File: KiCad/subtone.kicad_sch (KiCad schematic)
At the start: 10 parts, among them J1 7P Header, J2 Conn_01x07_Pin, J3 3P Header, SW1 Encoder, U1 MODULE-XIAO-RP2040

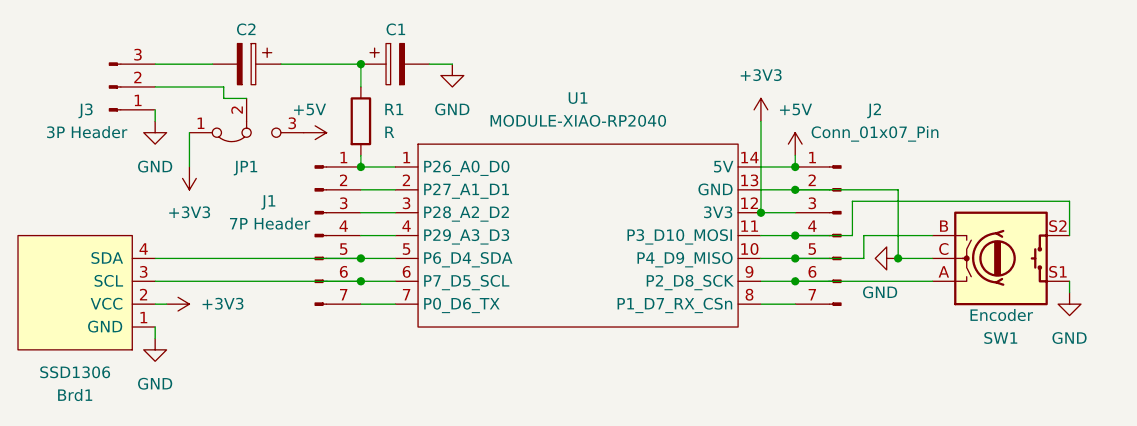
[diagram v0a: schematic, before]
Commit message: * Added screenshot * Default to 5V on J3 Header
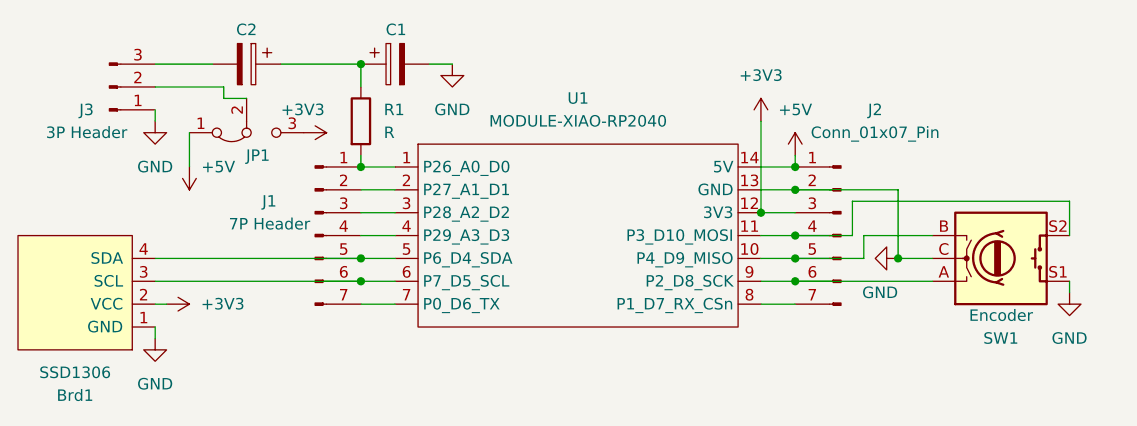
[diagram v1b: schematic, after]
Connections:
- net +3V3: now also JP1.3 (B); no longer JP1.1 (A)
- net +5V: now also JP1.1 (A); no longer JP1.3 (B)
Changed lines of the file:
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@@
+    )
+  )
+  (symbol (lib_id "power:+3V3") (at 83.82 34.29 270) (unit 1)
+    (in_bom yes) (on_board yes) (dnp no)
+    (property "Reference" "#PWR07" (at 80.01 34.29 0)
+      (effects (font (size 1.27 1.27)) hide)
+    )
+    (property "Value" "+3V3" (at 81.28 31.75 90)
+      (effects (font (size 1.27 1.27)) (justify left))
+    )
+    (property "Footprint" "" (at 83.82 34.29 0)
+      (effects (font (size 1.27 1.27)) hide)
+    )
+    (property "Datasheet" "" (at 83.82 34.29 0)
+      (effects (font (size 1.27 1.27)) hide)
+    )
+    (pin "1")
+    (instances
+      (project "subtone"
+        (path "/fb2bd3e4-75a5-4576-8ec5-6224bbfd73f9"
+          (reference "#PWR07") (unit 1)
+        )
+      )
     )
   )
@@
   (symbol (lib_id "Jumper:Jumper_3_Bridged12") (at 77.47 34.29 0) (mirror x) (unit 1)
     (in_bom yes) (on_board yes) (dnp no)
-    (property "Reference" "JP1" (at 77.47 38.1 0)
+    (property "Reference" "JP1" (at 78.74 36.83 0)
       (effects (font (size 1.27 1.27)))
     )
@@
     )
   )
-  (symbol (lib_id "power:+5V") (at 83.82 34.29 270) (unit 1)
-    (in_bom yes) (on_board yes) (dnp no)
-    (property "Reference" "#PWR07" (at 80.01 34.29 0)
-      (effects (font (size 1.27 1.27)) hide)
-    )
-    (property "Value" "+5V" (at 82.55 31.75 90)
-      (effects (font (size 1.27 1.27)) (justify left))
-    )
-    (property "Footprint" "" (at 83.82 34.29 0)
-      (effects (font (size 1.27 1.27)) hide)
-    )
-    (property "Datasheet" "" (at 83.82 34.29 0)
-      (effects (font (size 1.27 1.27)) hide)
-    )
-    (pin "1")
-    (instances
-      (project "subtone"
-        (path "/fb2bd3e4-75a5-4576-8ec5-6224bbfd73f9"
-          (reference "#PWR07") (unit 1)
-        )
-      )
-    )
-  )
   (symbol (lib_id "power:GND") (at 168.91 52.07 0) (unit 1)
     (in_bom yes) (on_board yes) (dnp no) (fields_autoplaced)
@@
         (path "/fb2bd3e4-75a5-4576-8ec5-6224bbfd73f9"
           (reference "#PWR06") (unit 1)
+        )
+      )
+    )
+  )
+  (symbol (lib_id "power:+5V") (at 71.12 38.1 180) (unit 1)
+    (in_bom yes) (on_board yes) (dnp no)
+    (property "Reference" "#PWR09" (at 71.12 34.29 0)
+      (effects (font (size 1.27 1.27)) hide)
+    )
+    (property "Value" "+5V" (at 76.2 38.1 0)
+      (effects (font (size 1.27 1.27)) (justify left))
+    )
+    (property "Footprint" "" (at 71.12 38.1 0)
+      (effects (font (size 1.27 1.27)) hide)
+    )
+    (property "Datasheet" "" (at 71.12 38.1 0)
+      (effects (font (size 1.27 1.27)) hide)
+    )
+    (pin "1")
+    (instances
+      (project "subtone"
+        (path "/fb2bd3e4-75a5-4576-8ec5-6224bbfd73f9"
+          (reference "#PWR09") (unit 1)
         )
       )
@@
         )
       )
-    )
-  )
-  (symbol (lib_id "power:+3V3") (at 71.12 38.1 180) (unit 1)
-    (in_bom yes) (on_board yes) (dnp no) (fields_autoplaced)
-    (property "Reference" "#PWR09" (at 71.12 34.29 0)
-      (effects (font (size 1.27 1.27)) hide)
-    )
-    (property "Value" "+3V3" (at 71.12 43.18 0)
-      (effects (font (size 1.27 1.27)))
-    )
-    (property "Footprint" "" (at 71.12 38.1 0)
-      (effects (font (size 1.27 1.27)) hide)
-    )
-    (property "Datasheet" "" (at 71.12 38.1 0)
-      (effects (font (size 1.27 1.27)) hide)
-    )
-    (pin "1")
-    (instances
-      (project "subtone"
-        (path "/fb2bd3e4-75a5-4576-8ec5-6224bbfd73f9"
-          (reference "#PWR09") (unit 1)
-        )
-      )

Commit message: Schematics and pcb updates
SDD1306 needs 5V and some devices need external i2c pull-ups.
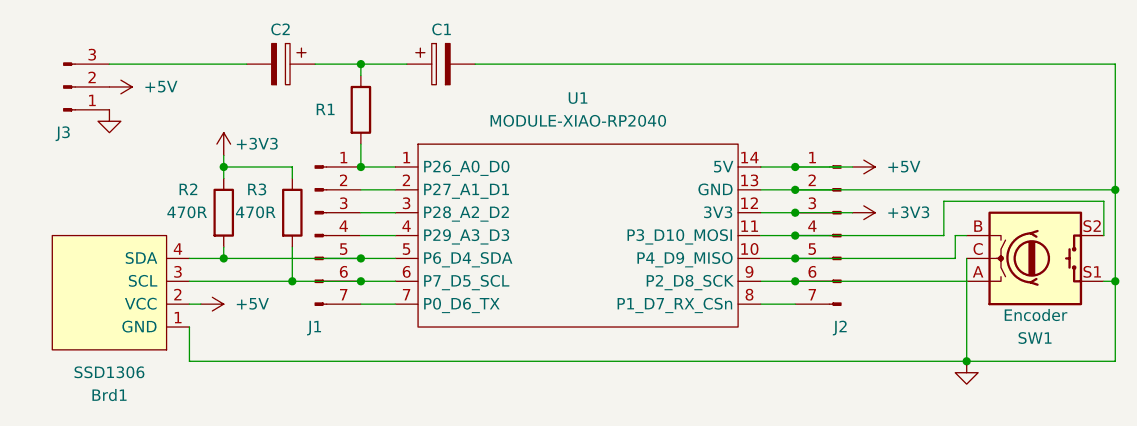
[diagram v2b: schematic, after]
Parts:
- removed JP1: Jumper_3_Bridged12, Jumper:SolderJumper-3_P1.3mm_Bridged2Bar12_Pad1.0x1.5mm, symbol Jumper:Jumper_3_Bridged12
- added R2, R3: 470R, Resistor_SMD:R_0805_2012Metric_Pad1.20x1.40mm_HandSolder, symbol Device:R
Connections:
- net +3V3: now also R2.1, R3.1; no longer Brd1.2 (VCC)
- net +5V: now also Brd1.2 (VCC), J3.2 (Pin_2)
- net at Brd1.4 (SDA), J1.5 (Pin_5), U1.5 (P6_D4_SDA): now also R2.2
- net at Brd1.3 (SCL), J1.6 (Pin_6), U1.6 (P7_D5_SCL): now also R3.2
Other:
- moved on the sheet: Brd1, C1, C2, J3, R1, SW1

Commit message: fixed resistor values
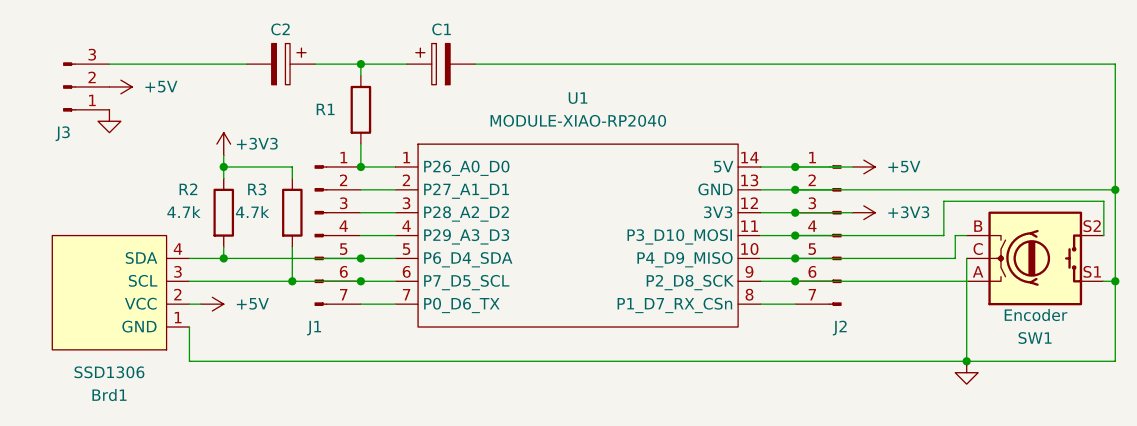
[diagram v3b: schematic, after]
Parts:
- R2, R3: value 470R -> 4.7k
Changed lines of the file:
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@@
       (effects (font (size 1.27 1.27)) (justify left))
     )
-    (property "Value" "470R" (at 76.2 43.18 0)
+    (property "Value" "4.7k" (at 76.2 43.18 0)
       (effects (font (size 1.27 1.27)) (justify left))
     )
@@
       (effects (font (size 1.27 1.27)) (justify left))
     )
-    (property "Value" "470R" (at 68.58 43.18 0)
+    (property "Value" "4.7k" (at 68.58 43.18 0)
       (effects (font (size 1.27 1.27)) (justify left))
     )
